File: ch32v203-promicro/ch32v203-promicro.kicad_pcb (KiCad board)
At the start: 2 copper layers, 17.8 x 33 mm, 27 parts, among them J1 USB2.0_C_v3, J2 ProMicro-LeftPin, J3 ProMicro-RightPin, SW1 SW_Push, SW2 SW_Push, U1 CH32V203CxT6, U2 AMS1117-3.3, Y1 32.768k, Y2 8M

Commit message: wip
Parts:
- C1, C10, C2, C3, C5, C6, C9, R1, R4, R5, R6, R7: moved to B.Cu
- U2, Y1: moved to F.Cu
- Y2: value 8M -> Crystal_GND24
- moved C9 53.8 mm to (105.5, 131.0), turned to -90 degrees
- moved C8 47.6 mm to (109.9, 131.0), turned to -90 degrees
- moved C7 47.2 mm to (107.9, 131.0), turned to -90 degrees
- moved R4 40.8 mm to (108.1, 102.0), turned to 90 degrees
- moved R5 40.5 mm to (110.2, 102.0), turned to 90 degrees
- moved C10 39.9 mm to (112.5, 131.0), turned to 90 degrees
- moved R7 31.1 mm to (106.3, 124.1), turned to -90 degrees
- moved R1 30.4 mm to (104.6, 110.7), turned to 90 degrees
- moved C2 29.9 mm to (107.6, 117.3)
- moved R6 29.4 mm to (103.6, 124.4), turned to -90 degrees
- moved C5 28.9 mm to (108.1, 112.4), turned to 180 degrees
- moved J3 27.9 mm to (116.5, 131.8), turned to 180 degrees
- moved C6 26.4 mm to (113.2, 127.9), turned to 180 degrees
- moved C3 24.5 mm to (107.4, 120.3), turned to 90 degrees
- moved C4 13.8 mm to (113.5, 109.1), turned to -90 degrees
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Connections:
- Y2 pad 2: Net-(C9-Pad1) -> GND
- Y2 pad 3: (no net) -> Net-(C9-Pad1)
- Y2 pad 4: (no net) -> GND
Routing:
- net +3V3: track 8.28 -> 42.2 mm, vias 0 -> 5
- net DM: track 0.00 -> 31.3 mm, vias 0 -> 4
- net DP: track 0.00 -> 28.9 mm, vias 0 -> 4
- net 10/A10: track 0.00 -> 24.6 mm, vias 0 -> 1
- net Net-(SW2-Pad2): track 0.00 -> 19.4 mm, vias 0 -> 2
- net 7: track 0.00 -> 18.5 mm, vias 0 -> 2
- net 1/UART_TX: track 0.00 -> 15.4 mm, vias 0 -> 1
- net +5V: track 0.00 -> 14.0 mm
- net 9/A9: track 0.00 -> 13.9 mm, vias 0 -> 1
- net 3/I2C_SCL: track 0.00 -> 13.9 mm, vias 0 -> 1
- net Net-(C10-Pad1): track 0.00 -> 13.8 mm, vias 0 -> 1
- net 5: track 0.00 -> 13.2 mm, vias 0 -> 1
- net 2/I2C_SDA: track 0.00 -> 13.2 mm, vias 0 -> 1
- net 0/UART_RX: track 0.00 -> 12.9 mm, vias 0 -> 1
- net 8/A8: track 0.00 -> 12.3 mm, vias 0 -> 1
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
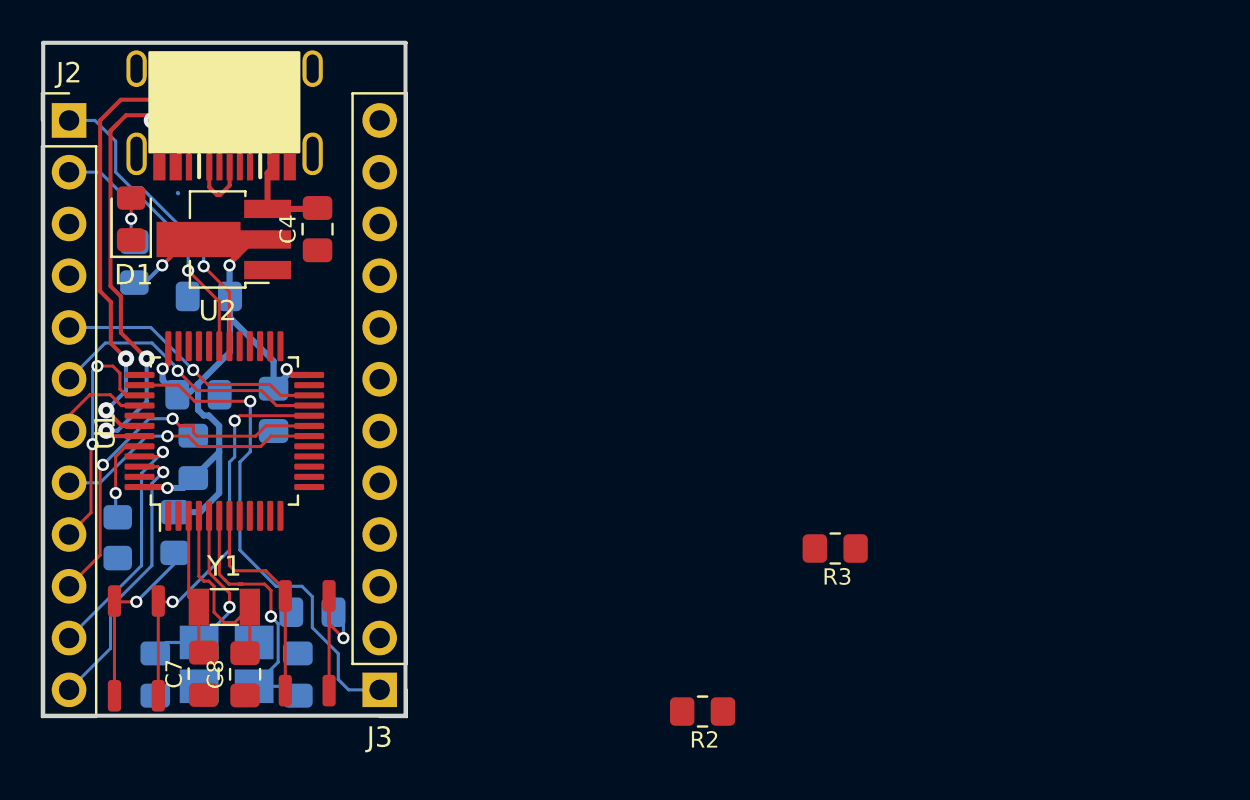
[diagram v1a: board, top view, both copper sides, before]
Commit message: ch32v203 promicro
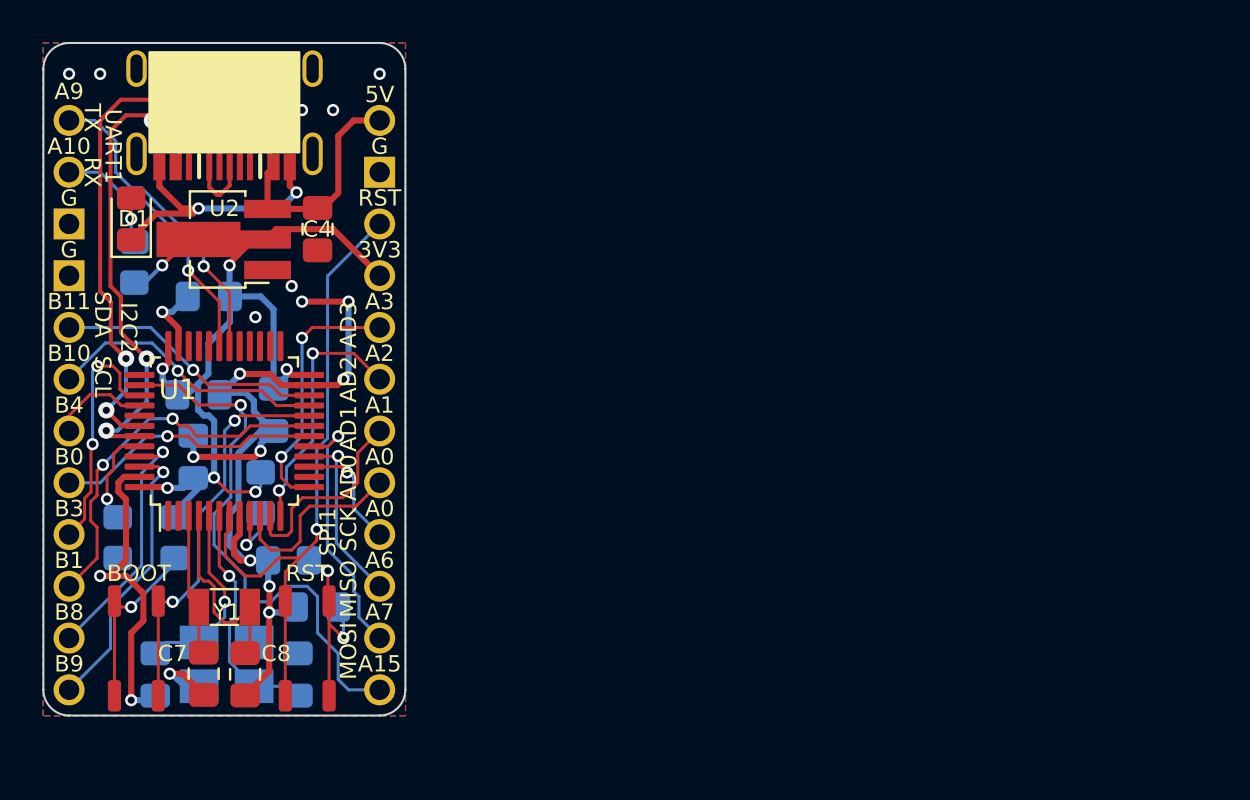
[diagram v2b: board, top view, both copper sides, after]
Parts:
- added REF**: JLCJLCJLCJLC, $74th:JLCJLCJLCJLC, B.Cu at (115.0, 108.1)
- J2: footprint Connector_PinHeader_2.54mm:PinHeader_1x12_P2.54mm_Vertical -> $74th:ProMicro_LIKE_LEFT
- J3: footprint Connector_PinHeader_2.54mm:PinHeader_1x12_P2.54mm_Vertical -> $74th:ProMicro_LIKE_RIGHT
- R2, R3: moved to B.Cu
- moved R3 28.5 mm to (110.6, 122.2), turned to -90 degrees
- moved R2 21.8 mm to (111.9, 125.3), turned to 180 degrees
- moved J2 14.0 mm to (101.3, 117.8)
- moved J3 12.7 mm to (116.5, 119.0), turned to 0 degrees
- moved C6 0.34 mm to (113.4, 127.7)
- moved R7 0.25 mm to (106.3, 124.4)
- moved SW1 0.25 mm to (113.0, 129.7)
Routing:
- net GND: track 0.00 -> 79.3 mm, vias 0 -> 23
- net RST: track 10.7 -> 31.3 mm, vias 0 -> 1
- net 21/A3: track 0.00 -> 12.9 mm, vias 0 -> 2
- net 16/SPI_MOSI: track 0.00 -> 12.8 mm, vias 0 -> 1
- net 20/A2: track 0.00 -> 12.5 mm, vias 0 -> 2
- net 19/A1: track 0.00 -> 9.91 mm
- net 18/A0: track 0.00 -> 9.35 mm
- net 14/SPI_MISO: track 0.00 -> 8.74 mm, vias 0 -> 1
- net +3V3: track 42.2 -> 50.6 mm, vias 5 -> 7
- net +5V: track 14.0 -> 20.4 mm
- net 15/SPI_SCK: track 0.00 -> 5.73 mm, vias 0 -> 1
- net Net-(R3-Pad2): track 0.00 -> 3.34 mm, vias 0 -> 1
- net 10/A10: track 24.6 -> 27.0 mm
- net Net-(C10-Pad1): track 13.8 -> 11.7 mm
- net DM: track 31.3 -> 30.2 mm
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- added copper zone on B.Cu, net GND
- added copper zone on F.Cu, net GND
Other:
- outline, holes or cut-outs redrawn
- board text added: "3V3"
- board text added: "5V"
- board text added: "A0"
- board text added: "A1"
- board text added: "A10"
- board text added: "A15"
- board text added: "A2"
- board text added: "A3"
- board text added: "A6"
- board text added: "A7"
- board text added: "A9"
- board text added: "AD0"
- board text added: "AD1"
- board text added: "AD2"
- board text added: "AD3"
- board text added: "B0"
- board text added: "B1"
- board text added: "B10"
- board text added: "B11"
- board text added: "B3"
- board text added: "B4"
- board text added: "B8"
- board text added: "B9"
- board text added: "BOOT"
- board text added: "C32V203Micro"
- board text added: "G"
- board text added: "I2C2"
- board text added: "MISO"
- board text added: "MOSI"
- board text added: "RST"
- board text added: "RX"
- board text added: "SCK"
- board text added: "SCL"
- board text added: "SDA"
- board text added: "SPI1"
- board text added: "TX"
- board text added: "UART1"
- board text added: "v1.0.0"
